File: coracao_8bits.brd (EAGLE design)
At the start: 78 x 72 mm, 70 parts, among them IC1 74HC595D, IC2 74HC595D, IC3 74HC595D, IC4 74HC595D, J1 FEMALE 2x3, U2 ATMEGA168, Y1 16MHZ

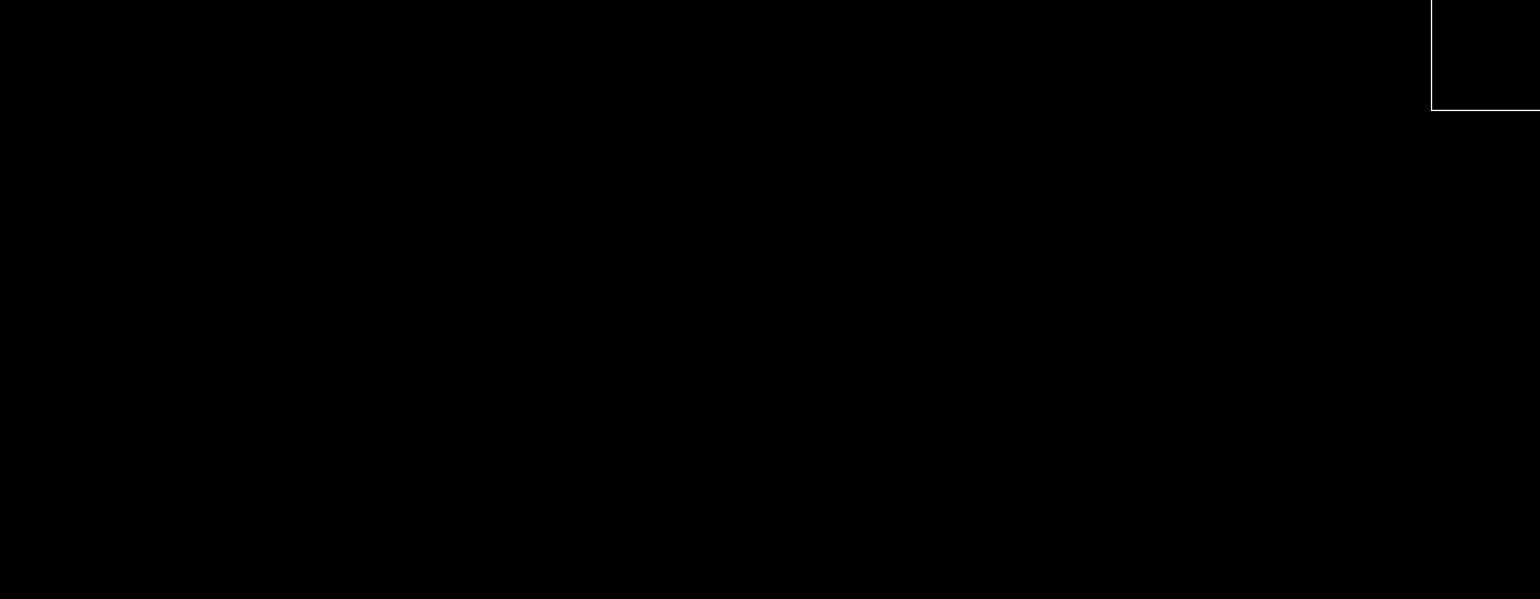
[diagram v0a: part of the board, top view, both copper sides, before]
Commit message: add power jack
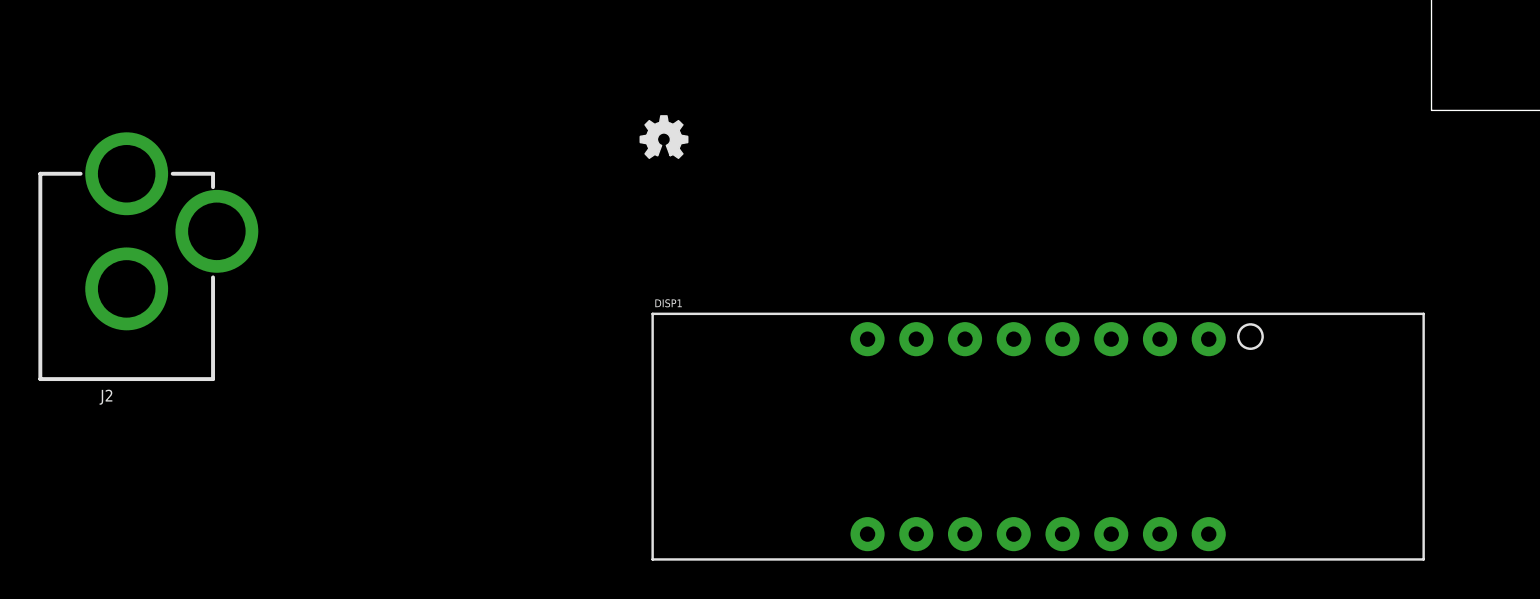
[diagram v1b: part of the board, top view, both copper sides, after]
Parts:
- added DISP1: YSD-439AR6B-35, SparkFun-LED:7-SEGMENT-4DIGIT-YOUNGSUN
- added J2: POWER_JACK, SparkFun-Connectors:POWER_JACK_PTH
- added LOGO1: OSHW-LOGOMINI, SparkFun-Aesthetics:OSHW-LOGO-MINI
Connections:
- removed net VIN: C1.A, U1.1, U1.3
- new net DEETE: C1.A, J2.PWR, U1.1, U1.3
- net GND: now also J2.GND, J2.GNDBREAK
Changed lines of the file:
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@@
 <attribute name="SF_SKU" value="COM-08229" x="15" y="4.1" size="1.778" layer="27" rot="R90" display="off"/>
+</element>
+<element name="LOGO1" library="SparkFun-Aesthetics" package="OSHW-LOGO-MINI" value="OSHW-LOGOMINI" x="-43" y="-37.5"/>
+<element name="DISP1" library="SparkFun-LED" package="7-SEGMENT-4DIGIT-YOUNGSUN" value="YSD-439AR6B-35" x="-23.5" y="-53">
+<attribute name="PROD_ID" value="COMP-09493" x="-23.5" y="-53" size="1.778" layer="27" display="off"/>
+</element>
+<element name="J2" library="SparkFun-Connectors" package="POWER_JACK_PTH" value="POWER_JACK" x="-71" y="-53">
+<attribute name="PROD_ID" value="CONN-08197" x="-71" y="-53" size="1.778" layer="27" display="off"/>
 </element>
 </elements>
@@
 <contactref element="J1" pad="1"/>
 <contactref element="S2" pad="2"/>
-<wire x1="18.5" y1="6.877" x2="18.5" y2="10.877" width="0" layer="19" extent="1-1"/>
-<wire x1="15" y1="7.25" x2="18.5" y2="6.877" width="0" layer="19" extent="1-1"/>
-<wire x1="18.5" y1="2.877" x2="18.5" y2="6.877" width="0" layer="19" extent="1-1"/>
-<wire x1="15.5" y1="13.877" x2="18.5" y2="10.877" width="0" layer="19" extent="1-1"/>
-<wire x1="53.345" y1="31.9734" x2="15.5" y2="13.877" width="0" layer="19" extent="1-16"/>
-<wire x1="11.8" y1="10.2" x2="53.345" y2="31.9734" width="0" layer="19" extent="1-16"/>
-<wire x1="8.8" y1="10.4999" x2="11.8" y2="10.2" width="0" layer="19" extent="1-1"/>
-<wire x1="9.65" y1="7.1" x2="8.8" y2="10.4999" width="0" layer="19" extent="1-1"/>
-<wire x1="48.265" y1="25.8266" x2="9.65" y2="7.1" width="0" layer="19" extent="1-16"/>
-<wire x1="48.835" y1="9.1734" x2="48.265" y2="25.8266" width="0" layer="19" extent="16-16"/>
-<wire x1="5.4" y1="0.75" x2="48.835" y2="9.1734" width="0" layer="19" extent="1-16"/>
-<wire x1="44.1926" y1="-14.7" x2="5.4" y2="0.75" width="0" layer="19" extent="1-1"/>
-<wire x1="43.755" y1="3.0266" x2="44.1926" y2="-14.7" width="0" layer="19" extent="1-16"/>
-<wire x1="-34.8266" y1="-20.135" x2="43.755" y2="3.0266" width="0" layer="19" extent="16-16"/>
-<wire x1="35.6074" y1="-15.5" x2="-34.8266" y2="-20.135" width="0" layer="19" extent="1-16"/>
-<wire x1="35.6074" y1="-13.9" x2="35.6074" y2="-15.5" width="0" layer="19" extent="1-1"/>
-<wire x1="-7.084" y1="-2.6" x2="35.6074" y2="-15.5" width="0" layer="19" extent="1-1"/>
+<contactref element="J2" pad="GNDBREAK"/>
+<contactref element="J2" pad="GND"/>
+<wire x1="-66.3" y1="-42.3" x2="-71" y2="-45.3" width="0" layer="19" extent="1-1"/>
+<wire x1="-40.9734" y1="-15.055" x2="-66.3" y2="-42.3" width="0" layer="19" extent="16-16"/>
+<wire x1="-34.8266" y1="-20.135" x2="-40.9734" y2="-15.055" width="0" layer="19" extent="16-16"/>
+<wire x1="-12.377" y1="-5" x2="-34.8266" y2="-20.135" width="0" layer="19" extent="1-16"/>
+<wire x1="-9.116" y1="-2.6" x2="-12.377" y2="-5" width="0" layer="19" extent="1-1"/>
 <wire x1="-8.1" y1="0.15" x2="-8.1" y2="-2.6" width="0" layer="19" extent="1-1"/>
-<wire x1="-40.9734" y1="-15.055" x2="-8.1" y2="0.15" width="0" layer="19" extent="1-16"/>
-<wire x1="5.7" y1="12.98" x2="8.8" y2="10.4999" width="0" layer="19" extent="1-1"/>
-<wire x1="8.05" y1="14.9" x2="5.7" y2="12.98" width="0" layer="19" extent="1-1"/>
-<wire x1="7.377" y1="17" x2="8.05" y2="14.9" width="0" layer="19" extent="1-1"/>
-<wire x1="10.623" y1="17" x2="7.377" y2="17" width="0" layer="19" extent="1-1"/>
-<wire x1="2.5" y1="13.877" x2="5.7" y2="12.98" width="0" layer="19" extent="1-1"/>
-<wire x1="-12.377" y1="-5" x2="-9.116" y2="-2.6" width="0" layer="19" extent="1-1"/>
-<wire x1="-25.877" y1="35" x2="-12.377" y2="-5" width="0" layer="19" extent="1-1"/>
 <wire x1="-9.377" y1="-8" x2="-12.377" y2="-5" width="0" layer="19" extent="1-1"/>
 <wire x1="-6.377" y1="-11" x2="-9.377" y2="-8" width="0" layer="19" extent="1-1"/>
@@
 <wire x1="1.623" y1="-14" x2="-0.877" y2="-17.4" width="0" layer="19" extent="1-1"/>
 <wire x1="4.623" y1="-11" x2="1.623" y2="-14" width="0" layer="19" extent="1-1"/>
-<wire x1="29.5" y1="-22.2" x2="4.623" y2="-11" width="0" layer="19" extent="1-1"/>
 <wire x1="7.623" y1="-8" x2="4.623" y2="-11" width="0" layer="19" extent="1-1"/>
 <wire x1="10.623" y1="-5" x2="7.623" y2="-8" width="0" layer="19" extent="1-1"/>
 <wire x1="13.623" y1="-2" x2="10.623" y2="-5" width="0" layer="19" extent="1-1"/>
+<wire x1="18.5" y1="2.877" x2="13.623" y2="-2" width="0" layer="19" extent="1-1"/>
+<wire x1="18.5" y1="6.877" x2="18.5" y2="2.877" width="0" layer="19" extent="1-1"/>
+<wire x1="15" y1="7.25" x2="18.5" y2="6.877" width="0" layer="19" extent="1-1"/>
+<wire x1="18.5" y1="10.877" x2="18.5" y2="6.877" width="0" layer="19" extent="1-1"/>
+<wire x1="15.5" y1="13.877" x2="18.5" y2="10.877" width="0" layer="19" extent="1-1"/>
+<wire x1="11.8" y1="10.2" x2="15" y2="7.25" width="0" layer="19" extent="1-1"/>
+<wire x1="8.8" y1="10.4999" x2="11.8" y2="10.2" width="0" layer="19" extent="1-1"/>
+<wire x1="9.65" y1="7.1" x2="8.8" y2="10.4999" width="0" layer="19" extent="1-1"/>
+<wire x1="5.7" y1="12.98" x2="8.8" y2="10.4999" width="0" layer="19" extent="1-1"/>
+<wire x1="8.05" y1="14.9" x2="5.7" y2="12.98" width="0" layer="19" extent="1-1"/>
+<wire x1="7.377" y1="17" x2="8.05" y2="14.9" width="0" layer="19" extent="1-1"/>
+<wire x1="10.623" y1="17" x2="7.377" y2="17" width="0" layer="19" extent="1-1"/>
+<wire x1="2.5" y1="13.877" x2="5.7" y2="12.98" width="0" layer="19" extent="1-1"/>
 <wire x1="-0.877" y1="10.9" x2="2.5" y2="13.877" width="0" layer="19" extent="1-1"/>
 <wire x1="-2.5" y1="13.877" x2="-0.877" y2="10.9" width="0" layer="19" extent="1-1"/>
-<wire x1="-15.455" y1="25.4734" x2="-2.5" y2="13.877" width="0" layer="19" extent="1-16"/>
-<wire x1="-0.777" y1="23.2" x2="-15.455" y2="25.4734" width="0" layer="19" extent="1-16"/>
+<wire x1="5.4" y1="0.75" x2="9.65" y2="7.1" width="0" layer="19" extent="1-1"/>
+<wire x1="-0.777" y1="23.2" x2="-2.5" y2="13.877" width="0" layer="19" extent="1-1"/>
 <wire x1="-5.123" y1="29" x2="-0.777" y2="23.2" width="0" layer="19" extent="1-1"/>
-<wire x1="-20.535" y1="19.3266" x2="-40.9734" y2="-15.055" width="0" layer="19" extent="16-16"/>
-<wire x1="-20.623" y1="35" x2="-25.877" y2="35" width="0" layer="19" extent="1-1"/>
-<wire x1="-17.123" y1="35" x2="-20.623" y2="35" width="0" layer="19" extent="1-1"/>
-<wire x1="-13.623" y1="35" x2="-17.123" y2="35" width="0" layer="19" extent="1-1"/>
-<wire x1="-11.877" y1="35" x2="-13.623" y2="35" width="0" layer="19" extent="1-1"/>
+<wire x1="-11.877" y1="35" x2="-5.123" y2="29" width="0" layer="19" extent="1-1"/>
+<wire x1="-13.623" y1="35" x2="-11.877" y2="35" width="0" layer="19" extent="1-1"/>
+<wire x1="-17.123" y1="35" x2="-13.623" y2="35" width="0" layer="19" extent="1-1"/>
+<wire x1="-20.623" y1="35" x2="-17.123" y2="35" width="0" layer="19" extent="1-1"/>
+<wire x1="-25.877" y1="35" x2="-20.623" y2="35" width="0" layer="19" extent="1-1"/>
+<wire x1="-15.455" y1="25.4734" x2="-17.123" y2="35" width="0" layer="19" extent="1-16"/>
+<wire x1="-20.535" y1="19.3266" x2="-15.455" y2="25.4734" width="0" layer="19" extent="16-16"/>
+<wire x1="35.6074" y1="-13.9" x2="18.5" y2="2.877" width="0" layer="19" extent="1-1"/>
+<wire x1="35.6074" y1="-15.5" x2="35.6074" y2="-13.9" width="0" layer="19" extent="1-1"/>
+<wire x1="44.1926" y1="-14.7" x2="35.6074" y2="-13.9" width="0" layer="19" extent="1-1"/>
+<wire x1="29.5" y1="-22.2" x2="35.6074" y2="-15.5" width="0" layer="19" extent="1-1"/>
+<wire x1="43.755" y1="3.0266" x2="44.1926" y2="-14.7" width="0" layer="19" extent="1-16"/>
+<wire x1="48.835" y1="9.1734" x2="43.755" y2="3.0266" width="0" layer="19" extent="16-16"/>
+<wire x1="48.265" y1="25.8266" x2="48.835" y2="9.1734" width="0" layer="19" extent="16-16"/>
+<wire x1="53.345" y1="31.9734" x2="48.265" y2="25.8266" width="0" layer="19" extent="16-16"/>
 </signal>
 <signal name="N$1">
@@
 <wire x1="-1.55" y1="7.8" x2="24.42" y2="-24.74" width="0" layer="19" extent="16-16"/>
 </signal>
-<signal name="VIN">
-<contactref element="U1" pad="1"/>
-<contactref element="U1" pad="3"/>
-<contactref element="C1" pad="A"/>
-<wire x1="9.75" y1="10.4999" x2="7.85" y2="10.4999" width="0" layer="19" extent="1-1"/>
-<wire x1="5.7" y1="10.18" x2="7.85" y2="10.4999" width="0" layer="19" extent="1-1"/>
-</signal>
 <signal name="N$32">
 <contactref element="LEDPWR" pad="C"/>
@@
 <wire x1="45.725" y1="25.8266" x2="-0.85" y2="11" width="0" layer="19" extent="16-16"/>
 </signal>
+<signal name="DEETE">
+<contactref element="U1" pad="1"/>
+<contactref element="U1" pad="3"/>
+<contactref element="C1" pad="A"/>
+<contactref element="J2" pad="PWR"/>
+<wire x1="5.7" y1="10.18" x2="-71" y2="-39.3" width="0" layer="19" extent="1-1"/>
+<wire x1="7.85" y1="10.4999" x2="5.7" y2="10.18" width="0" layer="19" extent="1-1"/>
+<wire x1="9.75" y1="10.4999" x2="7.85" y2="10.4999" width="0" layer="19" extent="1-1"/>
+</signal>
 </signals>
